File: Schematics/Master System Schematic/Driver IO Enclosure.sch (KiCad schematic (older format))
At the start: 3 parts, among them U11 CAN_Bus_Module, U12 KY-019

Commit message: Cooling Pump, TSMP container Updates
>Added Cooling pump relay
>Added Cooling pump
>Added +12V plug to TSMP container
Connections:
- new net: A3.~ (~~D9), U11.~ (Serial_Clock) (x6)
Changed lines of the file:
@@
 EESchema Schematic File Version 4
-LIBS:Master System Schematic-cache
 EELAYER 30 0
 EELAYER END

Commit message: Started Voltage tap pcbs
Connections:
- new net: A3.~ (~~D9), U11.~ (Serial_Clock) (x6)
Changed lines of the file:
@@
 $Descr A4 11693 8268
 encoding utf-8
-Sheet 5 13
+Sheet 5 17
 Title ""
 Date "2020-10-12"

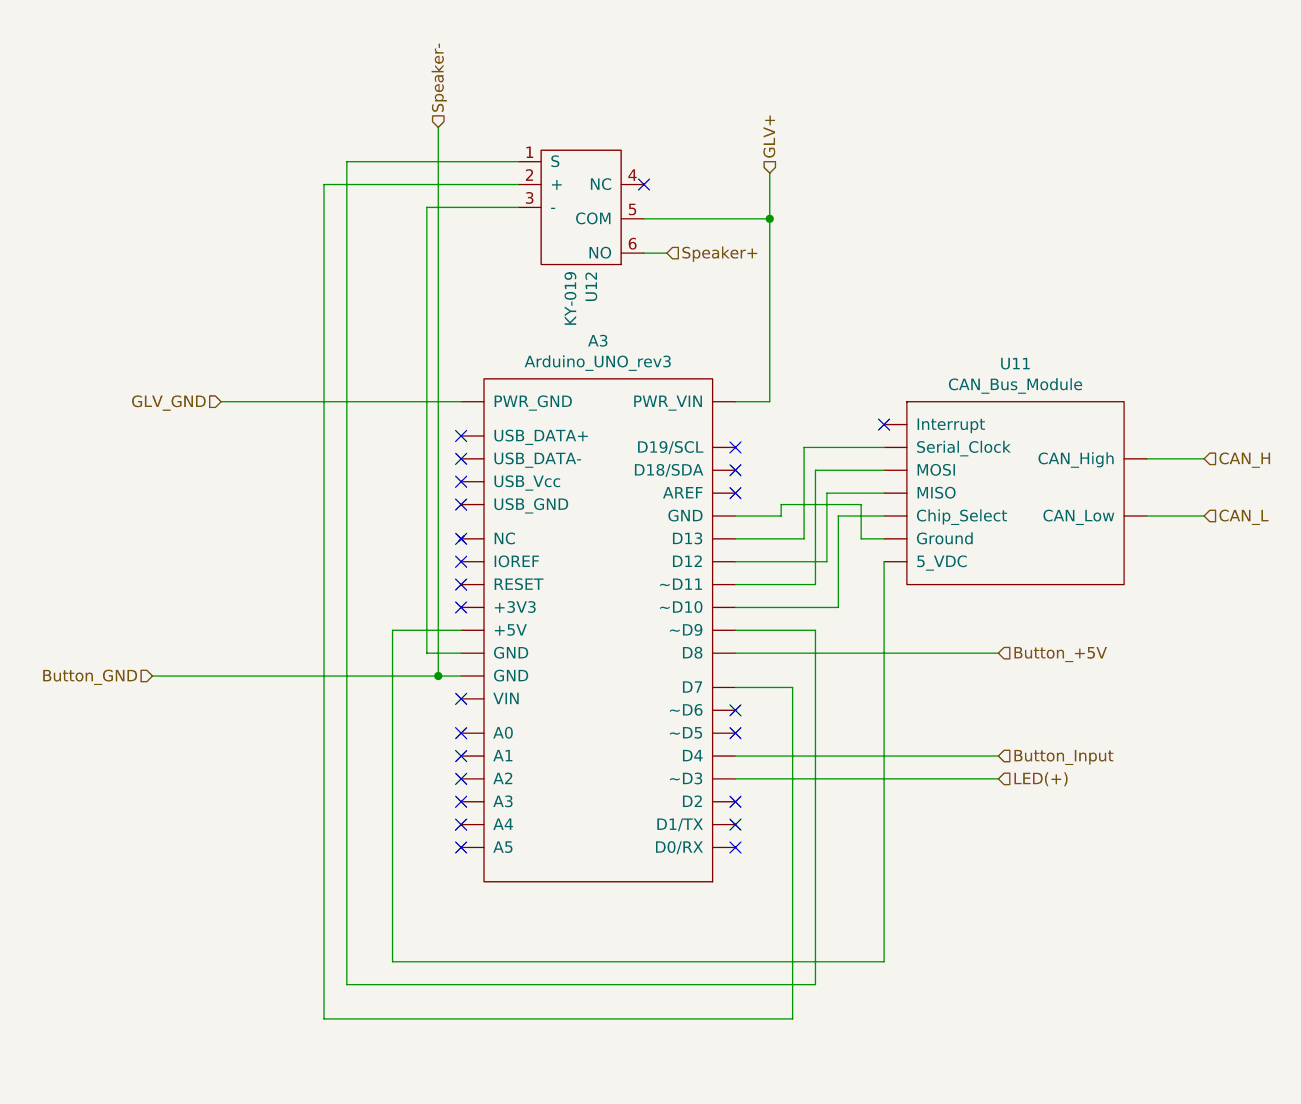
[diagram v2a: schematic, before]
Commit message: StartEnable w/ Voltage Divider
Added StartEnable wire to the dashboard can box and added a voltage divider with proper resistors to bring voltage down from 12V to 5V.
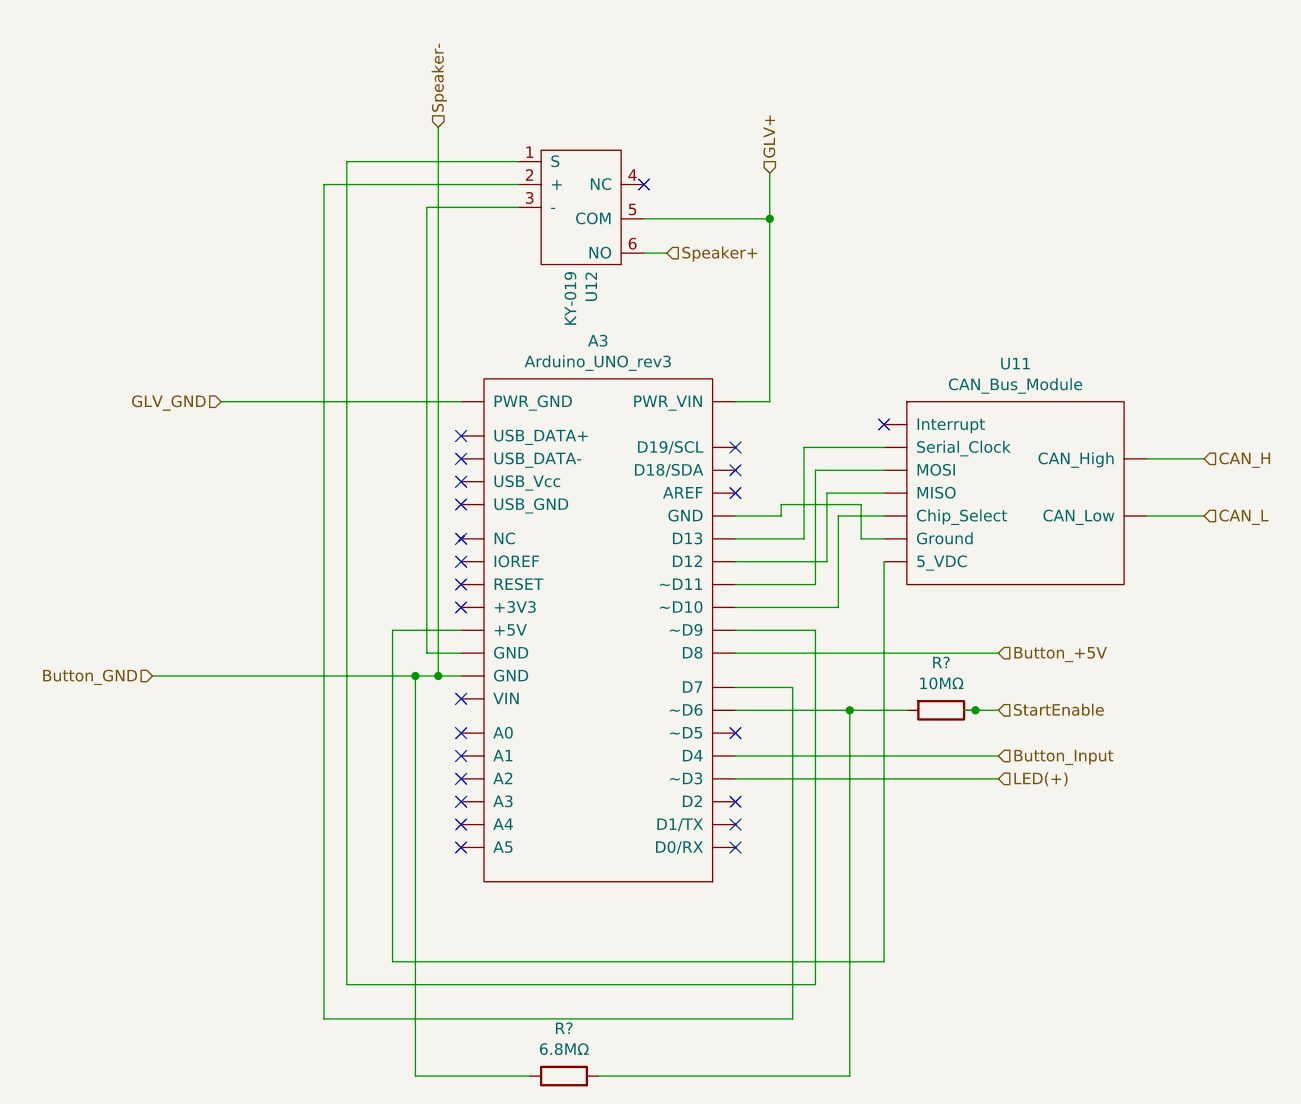
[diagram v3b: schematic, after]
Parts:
- added R?: 10MΩ, symbol Device:R
- added R?: 6.8MΩ, symbol Device:R
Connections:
- net Button_GND: now also R?.1
- new net: A3.~ (~~D9), U11.~ (Serial_Clock) (x6)
- new net: A3.~ (~~D9), R?.2, R?.2
- new net StartEnable: R?.1
- no-connect marks 25 -> 24
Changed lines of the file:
@@
 NoConn ~ 4850 4800
 NoConn ~ 4850 4900
-NoConn ~ 6050 4300
 NoConn ~ 6050 4400
 NoConn ~ 6050 4700
@@
 LED(+)
 Wire Wire Line
-	3500 4150 4750 4150
+	3500 4150 4650 4150
 Text HLabel 3500 4150 0    50   Input ~ 0
 Button_GND
@@
 Wire Wire Line
 	5650 2300 5750 2300
+Text HLabel 7200 4300 2    50   Input ~ 0
+StartEnable
+$Comp
+L Device:R R?
+U 1 1 5F8BB898
+P 6950 4300
+F 0 "R?" V 6743 4300 50  0000 C CNN
+F 1 "10MΩ" V 6834 4300 50  0000 C CNN
+F 2 "" V 6880 4300 50  0001 C CNN
+F 3 "~" H 6950 4300 50  0001 C CNN
+	1    6950 4300
+	0    1    1    0
+$EndComp
+Wire Wire Line
+	7200 4300 7100 4300
+Connection ~ 7100 4300
+Wire Wire Line
+	7100 4300 7050 4300
+Wire Wire Line
+	6050 4300 6550 4300
+$Comp
+L Device:R R?
+U 1 1 5F8C0C28
+P 5300 5900
+F 0 "R?" V 5507 5900 50  0000 C CNN
+F 1 "6.8MΩ" V 5416 5900 50  0000 C CNN
+F 2 "" V 5230 5900 50  0001 C CNN
+F 3 "~" H 5300 5900 50  0001 C CNN
+	1    5300 5900
+	0    -1   -1   0
+$EndComp
+Wire Wire Line
+	6550 4300 6550 5900
+Wire Wire Line
+	6550 5900 5450 5900
+Connection ~ 6550 4300
+Wire Wire Line
+	6550 4300 6800 4300
+Wire Wire Line
+	4650 5900 4650 4150
+Wire Wire Line
+	4650 5900 5150 5900
+Connection ~ 4650 4150
+Wire Wire Line
+	4650 4150 4750 4150
 $EndSCHEMATC

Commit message: Fixed Pin and Updated Title Block
-Fixed incorrectly imported pin
-Actually wired the pin in the master schematic
-Updated title block
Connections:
- new net: A3.~ (~~D9), U11.~ (Serial_Clock) (x6)
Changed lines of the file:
@@
 EESchema Schematic File Version 4
+LIBS:Master System Schematic-cache
 EELAYER 30 0
 EELAYER END

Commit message: Further fixing merge
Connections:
- new net: A3.~ (~~D9), U11.~ (Serial_Clock) (x6)
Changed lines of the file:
@@
 $Descr A4 11693 8268
 encoding utf-8
-Sheet 5 17
+Sheet 5 18
 Title ""
 Date "2020-10-12"

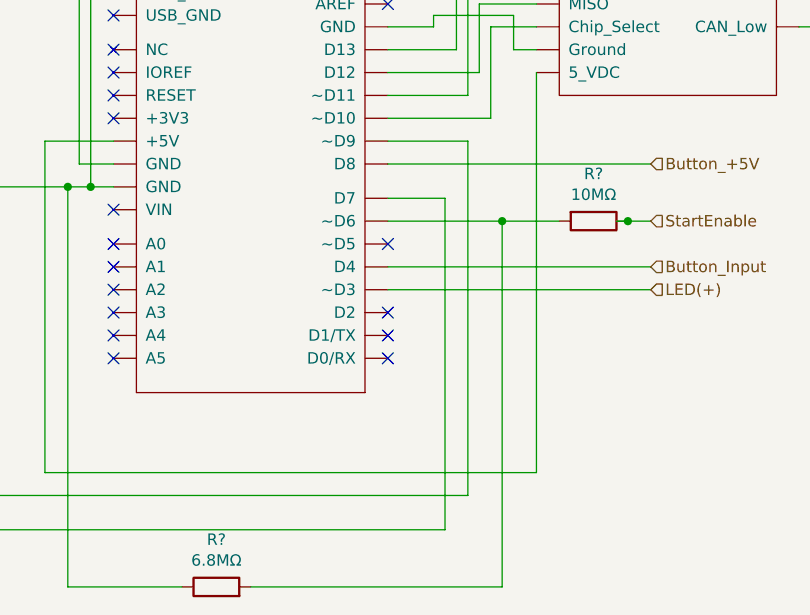
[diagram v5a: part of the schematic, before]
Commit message: cleanup on VT pcbs
>made vt relay boards much cleaner
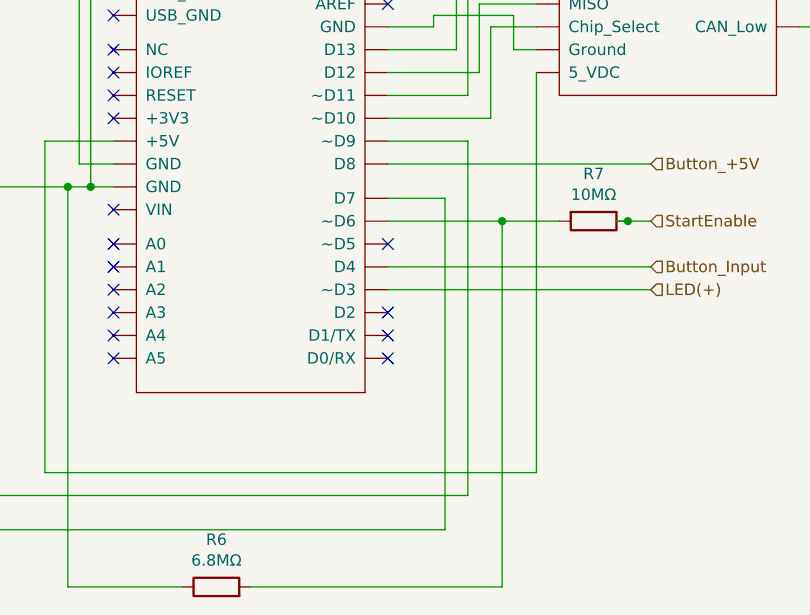
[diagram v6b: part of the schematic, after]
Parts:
- gave numbers to parts that had none: 2
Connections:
- new net: A3.~ (~~D9), U11.~ (Serial_Clock) (x6)
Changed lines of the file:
@@
 EESchema Schematic File Version 4
-LIBS:Master System Schematic-cache
 EELAYER 30 0
 EELAYER END
@@
 StartEnable
 $Comp
-L Device:R R?
+L Device:R R7
 U 1 1 5F8BB898
 P 6950 4300
-F 0 "R?" V 6743 4300 50  0000 C CNN
+F 0 "R7" V 6743 4300 50  0000 C CNN
 F 1 "10MΩ" V 6834 4300 50  0000 C CNN
 F 2 "" V 6880 4300 50  0001 C CNN
@@
 	6050 4300 6550 4300
 $Comp
-L Device:R R?
+L Device:R R6
 U 1 1 5F8C0C28
 P 5300 5900
-F 0 "R?" V 5507 5900 50  0000 C CNN
+F 0 "R6" V 5507 5900 50  0000 C CNN
 F 1 "6.8MΩ" V 5416 5900 50  0000 C CNN
 F 2 "" V 5230 5900 50  0001 C CNN

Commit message: FINISHED Voltage tap PCB schem
>reran battery box to fit new schem
>added placeholder thermistor board schem.
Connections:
- new net: A3.~ (~~D9), U11.~ (Serial_Clock) (x6)
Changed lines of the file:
@@
 $Descr A4 11693 8268
 encoding utf-8
-Sheet 5 18
+Sheet 5 21
 Title ""
 Date "2020-10-12"
